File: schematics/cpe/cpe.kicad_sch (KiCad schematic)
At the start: 163 parts

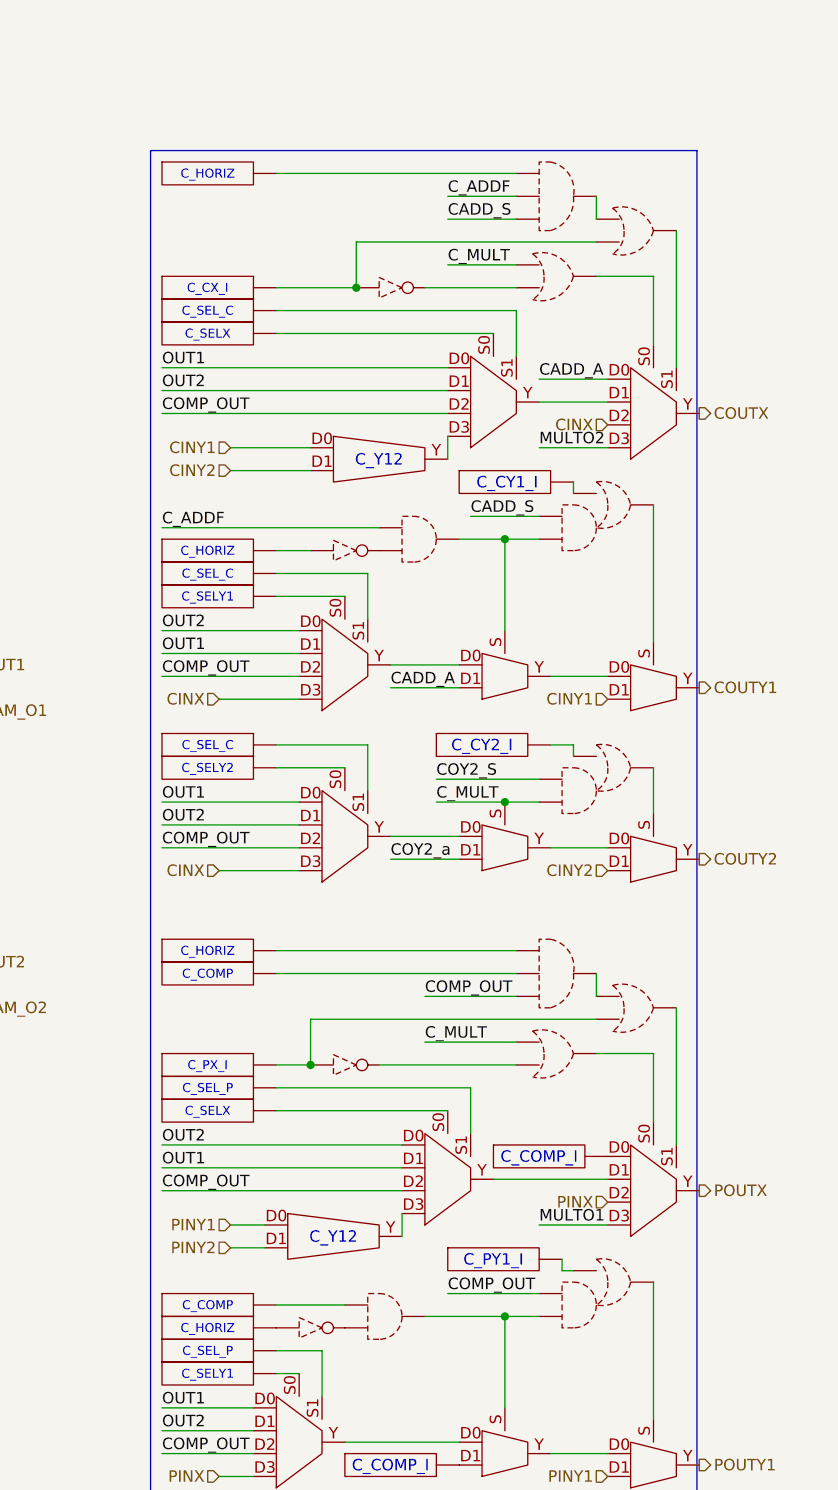
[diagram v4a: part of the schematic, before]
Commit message: fix C/P line errata caused by misunderstanding inversion
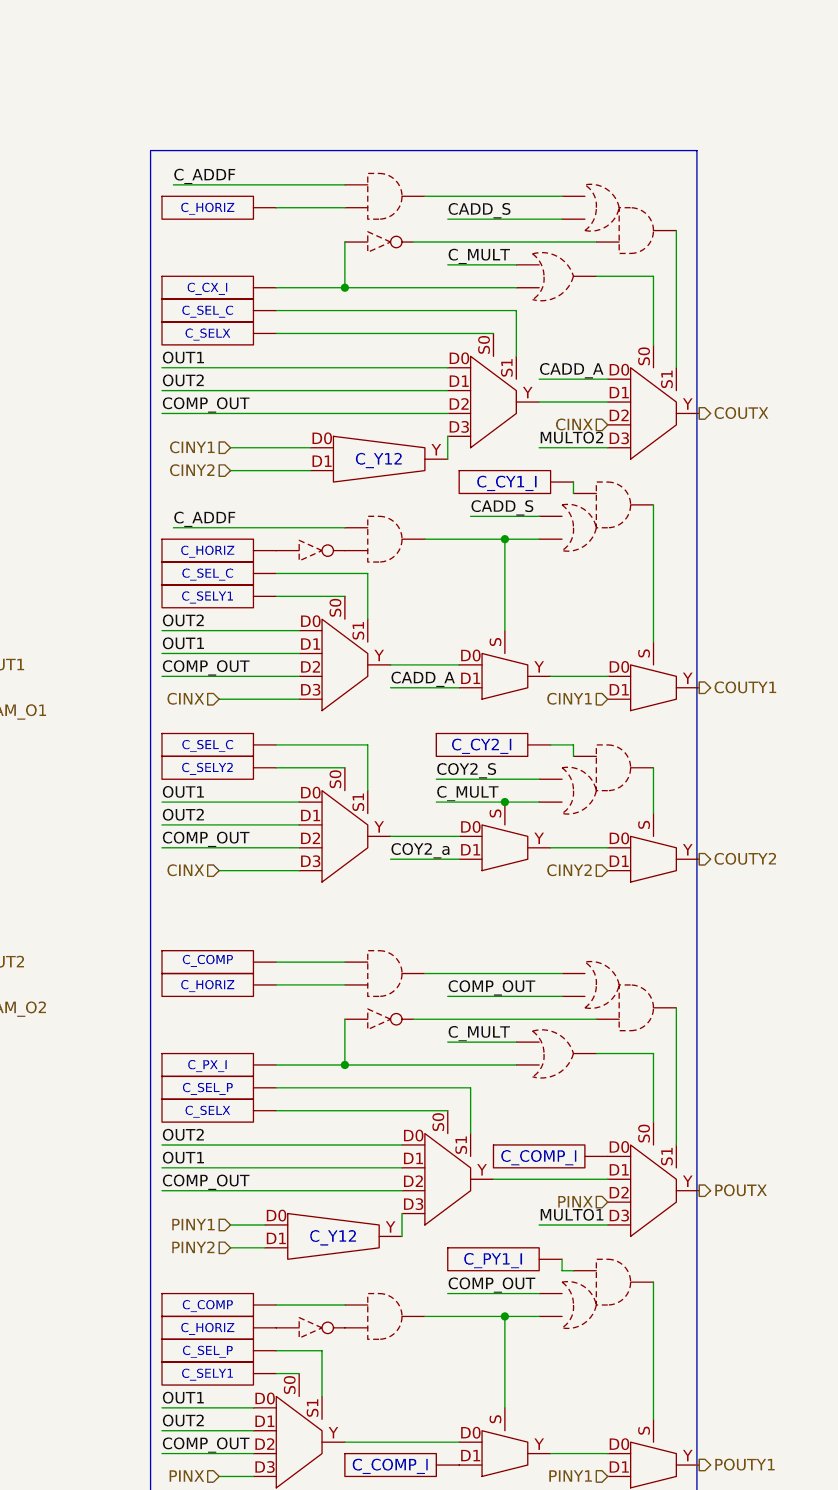
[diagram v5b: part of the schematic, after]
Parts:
- removed U1430, U1431: ~, symbol peppercorn:AND3
- removed U1434, U1435, U1436: ~, symbol peppercorn:OA21
- removed U1438, U1439: ~, symbol peppercorn:OR
- added U1224, U1225: ~, symbol peppercorn:AND
- added U147, U148, U151, U152, U153: ~, symbol peppercorn:AO21
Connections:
- net CADD_S: now also U147., U151.
- net COMP_OUT: now also U148., U153.
- net COY2_S: now also U152.
- net C_ADDF: now also U1224.
- net C_MULT: now also U152.
- net at M541.S: now also U152.
- net at U107.: now also U1225.
- net at U1425.: now also U152.
- net at U103., U1420.: now also U1433.
- net at M538.S, U114.: now also U153.
- net at M536.S, U1424.: now also U151.
- net at U1419.: now also U73.; no longer U1424.
- net at M542.S1: now also U148.
- net at U77.: now also U1362.A; no longer U67.
- net at U1422.: now also U147.; no longer U1432.
- net at U79.: now also L291.Y; no longer U24.
- net at M540.S: now also U151.
- net at U1427.: now also U151.
- net at U1426.: now also U153.
- net at M543.S: now also U153.
- net at U1399., U1422.: now also U1432.
- net at U1398.: now also U1224.
- net at M539.S1: now also U147.
- net at U108.: now also U1225.
- new net: U1367., U1370.
- new net: M523.D0, U1351., U1369.
- new net: U1420., U148.
- new net: U1225., U148.
- new net: U1419., U1424.
- new net: M524.S, U1365., U1371., U1372.
- new net: U82., U87.
- new net: U67., U77.
- new net: U1224., U147.
- new net: U24., U79.
- new net: M523.S, U1369., U1372., U1373.
- new net: U1366., U1368., U1369.
- new net: U83., U88.
